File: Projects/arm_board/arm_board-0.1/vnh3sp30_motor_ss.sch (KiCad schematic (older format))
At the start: 7 parts, among them P1 CONN_5, U28 74HC08

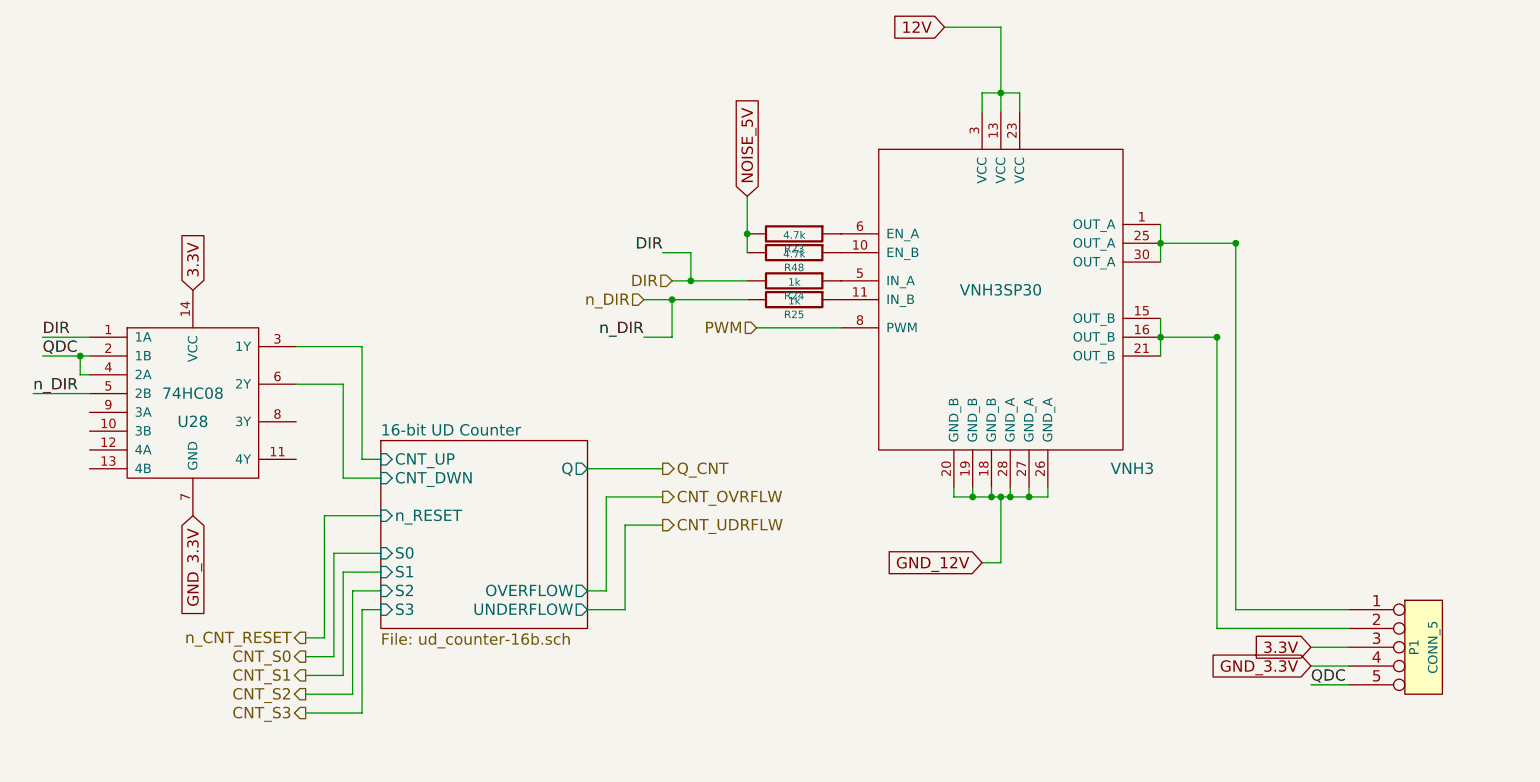
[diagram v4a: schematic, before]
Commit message: Arm Board: finish pcb layout, make gerbers
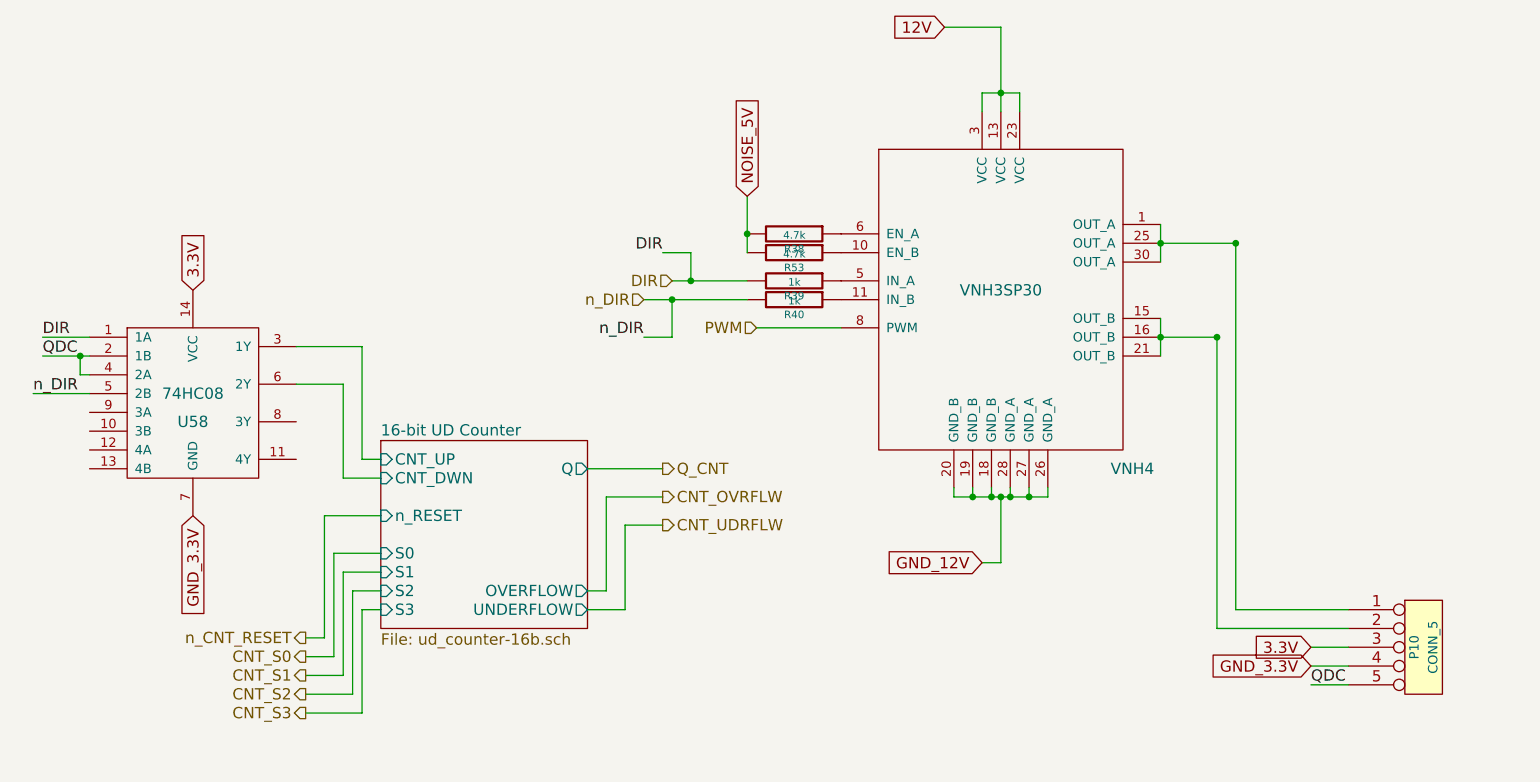
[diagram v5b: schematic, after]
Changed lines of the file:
@@
 AR Path="/56F55E0D/564A6239" Ref="VNH6"  Part="1"
 AR Path="/56F56B2F/564A6239" Ref="VNH7"  Part="1"
-F 0 "VNH3" H 9250 2850 60  0000 C CNN
+F 0 "VNH4" H 9250 2850 60  0000 C CNN
 F 1 "VNH3SP30" H 8550 3800 60  0000 C CNN
 F 2 "ArmFootprints:VNH3SP30TR-E" H 6950 3600 60  0001 C CNN
@@
 AR Path="/56F55E0D/56C5F3D4" Ref="R30"  Part="1"
 AR Path="/56F56B2F/56C5F3D4" Ref="R33"  Part="1"
-F 0 "R24" V 7530 3750 40  0000 C CNN
+F 0 "R39" V 7530 3750 40  0000 C CNN
 F 1 "1k" V 7457 3751 40  0000 C CNN
 F 2 "Resistors_SMD:R_0805" V 7380 3750 30  0001 C CNN
@@
 AR Path="/56F55E0D/56C5F9C5" Ref="R31"  Part="1"
 AR Path="/56F56B2F/56C5F9C5" Ref="R34"  Part="1"
-F 0 "R25" V 7530 3850 40  0000 C CNN
+F 0 "R40" V 7530 3850 40  0000 C CNN
 F 1 "1k" V 7457 3851 40  0000 C CNN
 F 2 "Resistors_SMD:R_0805" V 7380 3850 30  0001 C CNN
@@
 AR Path="/56F56B2F/56C6696F" Ref="R32"  Part="1"
 AR Path="/56F53B7D/56C6696F" Ref="R38"  Part="1"
-F 0 "R23" V 7530 3500 40  0000 C CNN
+F 0 "R38" V 7530 3500 40  0000 C CNN
 F 1 "4.7k" V 7457 3501 40  0000 C CNN
 F 2 "Resistors_SMD:R_0805" V 7380 3500 30  0001 C CNN
@@
 AR Path="/56F55E0D/56CA7E11" Ref="P7"  Part="1"
 AR Path="/56F56B2F/56CA7E11" Ref="P8"  Part="1"
-F 0 "P1" V 10750 5700 50  0000 C CNN
+F 0 "P10" V 10750 5700 50  0000 C CNN
 F 1 "CONN_5" V 10850 5700 50  0000 C CNN
 F 2 "ArmFootprints:5-pin_640467-1" H 10800 5700 60  0001 C CNN
@@
 AR Path="/56F55E0D/56CE991E" Ref="U42"  Part="1"
 AR Path="/56F56B2F/56CE991E" Ref="U44"  Part="1"
-F 0 "U28" H 4250 4200 60  0000 C CNN
+F 0 "U58" H 4250 4200 60  0000 C CNN
 F 1 "74HC08" H 4250 4350 60  0000 C CNN
 F 2 "ArmFootprints:SOIC-14" H 4250 4350 60  0001 C CNN
@@
 AR Path="/56F55E0D/56E620A0" Ref="R50"  Part="1"
 AR Path="/56F56B2F/56E620A0" Ref="R51"  Part="1"
-F 0 "R48" V 7530 3600 40  0000 C CNN
+F 0 "R53" V 7530 3600 40  0000 C CNN
 F 1 "4.7k" V 7457 3601 40  0000 C CNN
 F 2 "Resistors_SMD:R_0805" V 7380 3600 30  0001 C CNN
